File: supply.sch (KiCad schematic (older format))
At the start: 48 parts

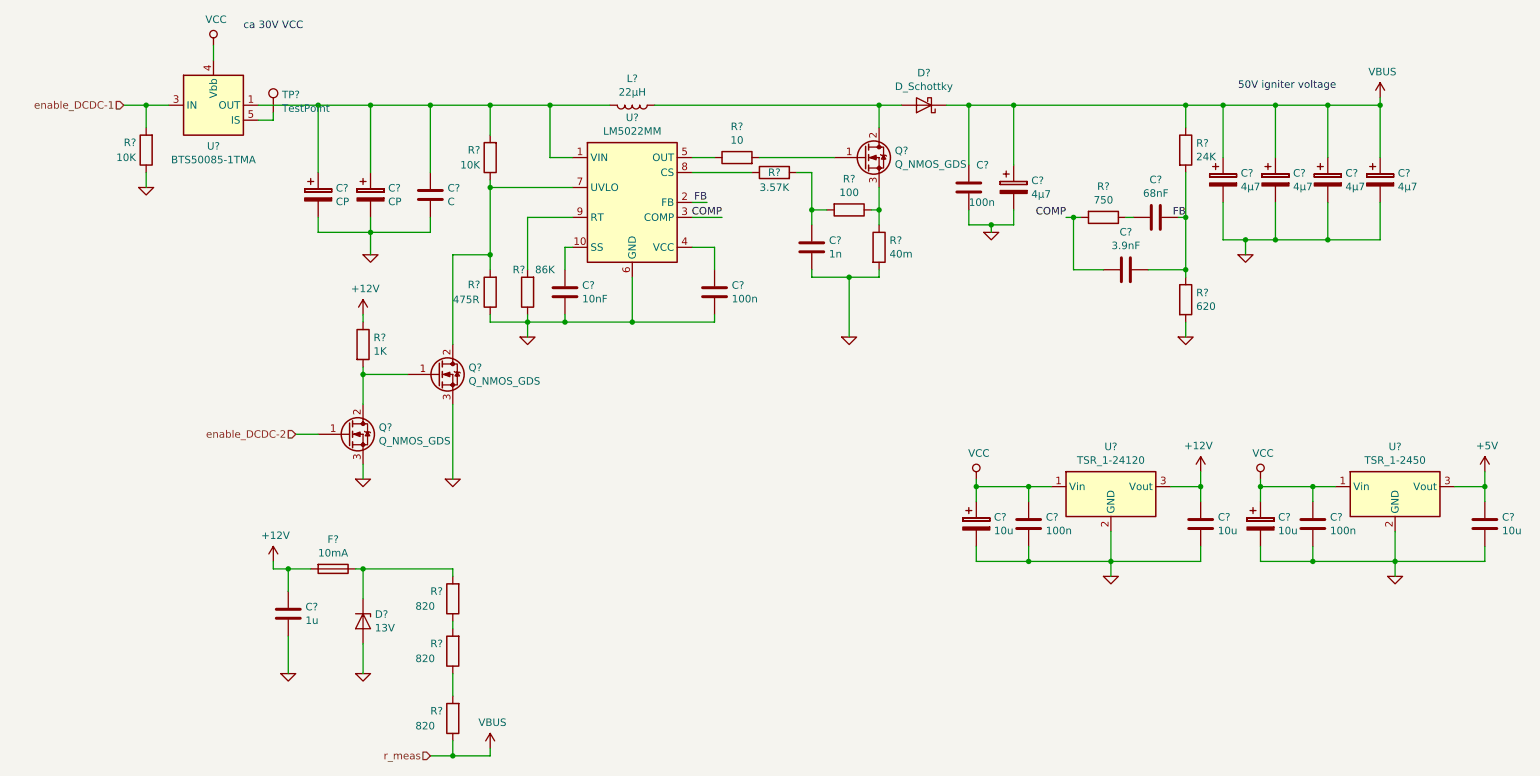
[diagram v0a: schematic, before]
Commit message: updated supply values
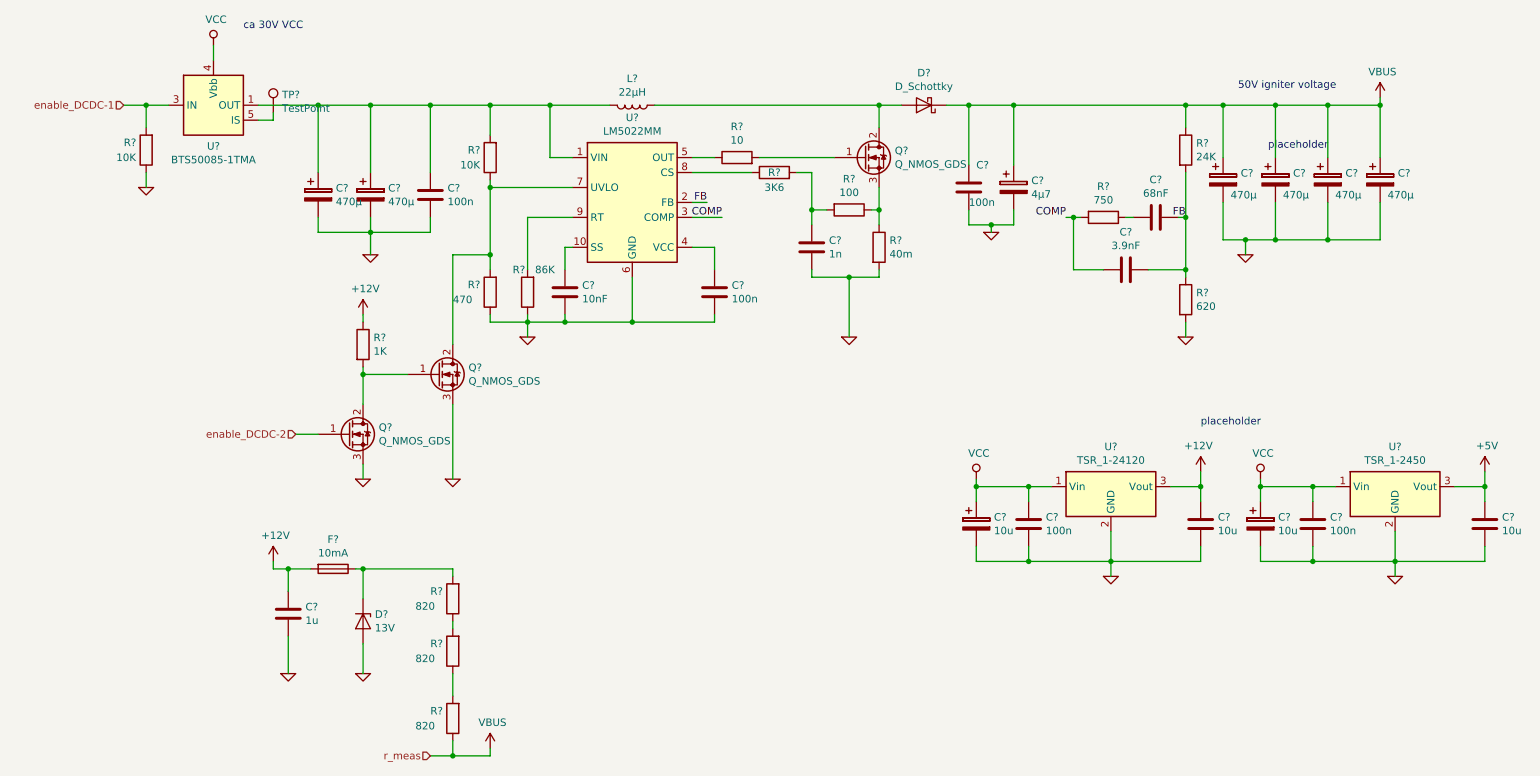
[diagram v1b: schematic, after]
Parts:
- C? (x4): value 4µ7 -> 470µ
- C?: value C -> 100n
- C? (x2): value CP -> 470µ
- R?: value 475R -> 470
- R?: value 3.57K -> 3K6
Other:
- note added: "placeholder\n"
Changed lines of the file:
@@
 P 4150 2450
 F 0 "R?" H 4300 2400 50  0000 R CNN
-F 1 "475R" H 4400 2500 50  0000 R CNN
+F 1 "470" H 4400 2500 50  0000 R CNN
 F 2 "" V 4080 2450 50  0001 C CNN
 F 3 "~" H 4150 2450 50  0001 C CNN
@@
 P 9050 1700
 F 0 "C?" H 9168 1746 50  0000 L CNN
-F 1 "4µ7" H 9168 1655 50  0000 L CNN
+F 1 "470µ" H 9100 1600 50  0000 L CNN
 F 2 "" H 9088 1550 50  0001 C CNN
 F 3 "~" H 9050 1700 50  0001 C CNN
@@
 P 9400 1700
 F 0 "C?" H 9518 1746 50  0000 L CNN
-F 1 "4µ7" H 9518 1655 50  0000 L CNN
+F 1 "470µ" H 9450 1600 50  0000 L CNN
 F 2 "" H 9438 1550 50  0001 C CNN
 F 3 "~" H 9400 1700 50  0001 C CNN
@@
 P 9750 1700
 F 0 "C?" H 9868 1746 50  0000 L CNN
-F 1 "4µ7" H 9868 1655 50  0000 L CNN
+F 1 "470µ" H 9800 1600 50  0000 L CNN
 F 2 "" H 9788 1550 50  0001 C CNN
 F 3 "~" H 9750 1700 50  0001 C CNN
@@
 P 10100 1700
 F 0 "C?" H 10218 1746 50  0000 L CNN
-F 1 "4µ7" H 10218 1655 50  0000 L CNN
+F 1 "470µ" H 10150 1600 50  0000 L CNN
 F 2 "" H 10138 1550 50  0001 C CNN
 F 3 "~" H 10100 1700 50  0001 C CNN
@@
 P 3750 1800
 F 0 "C?" H 3865 1846 50  0000 L CNN
-F 1 "C" H 3865 1755 50  0000 L CNN
+F 1 "100n" H 3865 1755 50  0000 L CNN
 F 2 "" H 3788 1650 50  0001 C CNN
 F 3 "~" H 3750 1800 50  0001 C CNN
@@
 P 3350 1800
 F 0 "C?" H 3468 1846 50  0000 L CNN
-F 1 "CP" H 3468 1755 50  0000 L CNN
+F 1 "470µ" H 3468 1755 50  0000 L CNN
 F 2 "" H 3388 1650 50  0001 C CNN
 F 3 "~" H 3350 1800 50  0001 C CNN
@@
 P 3000 1800
 F 0 "C?" H 3118 1846 50  0000 L CNN
-F 1 "CP" H 3118 1755 50  0000 L CNN
+F 1 "470µ" H 3118 1755 50  0000 L CNN
 F 2 "" H 3038 1650 50  0001 C CNN
 F 3 "~" H 3000 1800 50  0001 C CNN
@@
 P 6050 1650
 F 0 "R?" V 6050 1650 50  0000 C CNN
-F 1 "3.57K" V 5950 1650 50  0000 C CNN
+F 1 "3K6" V 5950 1650 50  0000 C CNN
 F 2 "" V 5980 1650 50  0001 C CNN
 F 3 "~" H 6050 1650 50  0001 C CNN
@@
 	3750 5550 3900 5550
 Connection ~ 3900 5550
+Text Notes 9350 1500 0    50   ~ 0
+placeholder\n
+Text Notes 8900 3350 0    50   ~ 0
+placeholder\n
 $EndSCHEMATC

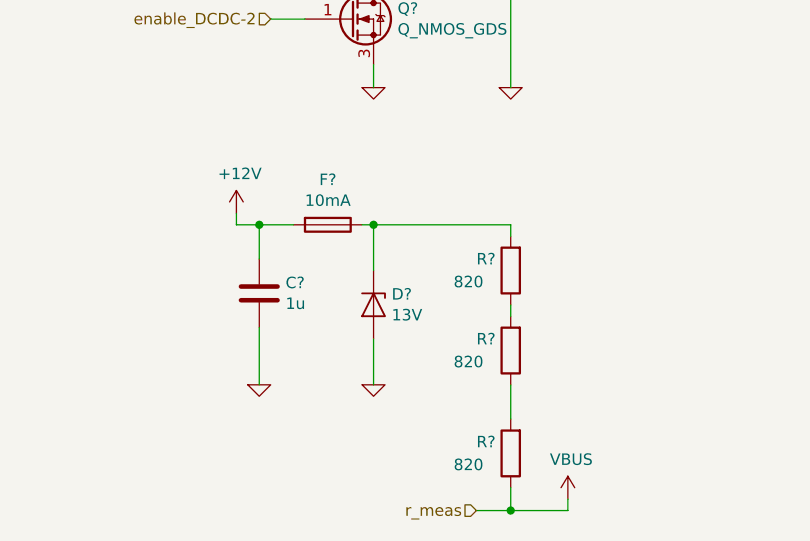
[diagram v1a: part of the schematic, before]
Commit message: added current measurement
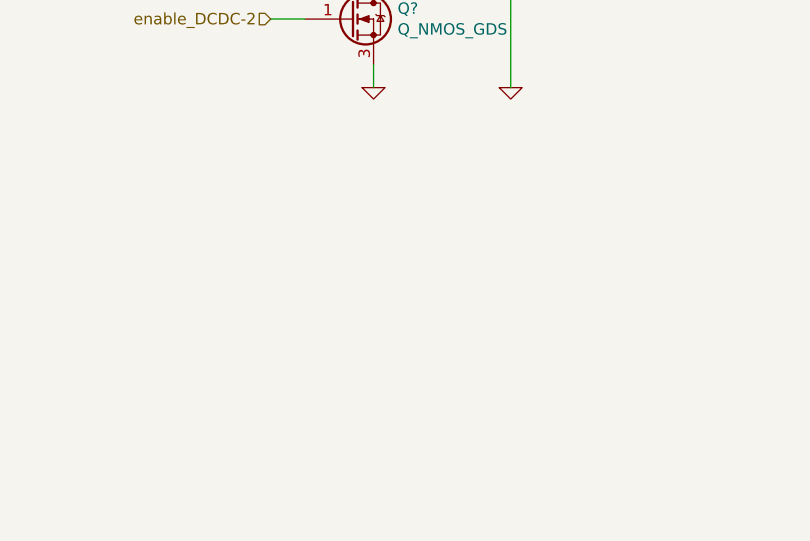
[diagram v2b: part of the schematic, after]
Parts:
- removed C?: 1u, symbol Device:C
- removed D?: 13V, symbol Device:D_Zener
- removed F?: 10mA, symbol Device:Fuse
- removed R? (x3): 820, symbol Device:R
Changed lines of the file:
@@
 $Descr A4 11693 8268
 encoding utf-8
-Sheet 3 4
+Sheet 3 5
 Title ""
 Date ""
@@
 Text HLabel 2850 3400 0    50   Input ~ 0
 enable_DCDC-2
-$Comp
-L Device:R R?
-U 1 1 5D2C7849
-P 3900 4500
-F 0 "R?" H 4050 4450 50  0000 R CNN
-F 1 "820" H 4150 4550 50  0000 R CNN
-F 2 "" V 3830 4500 50  0001 C CNN
-F 3 "~" H 3900 4500 50  0001 C CNN
-	1    3900 4500
-	-1   0    0    1
-$EndComp
-$Comp
-L Device:R R?
-U 1 1 5D2C79C2
-P 3900 4850
-F 0 "R?" H 4050 4800 50  0000 R CNN
-F 1 "820" H 4150 4900 50  0000 R CNN
-F 2 "" V 3830 4850 50  0001 C CNN
-F 3 "~" H 3900 4850 50  0001 C CNN
-	1    3900 4850
-	-1   0    0    1
-$EndComp
-$Comp
-L Device:R R?
-U 1 1 5D2C7AB2
-P 3900 5300
-F 0 "R?" H 4050 5250 50  0000 R CNN
-F 1 "820" H 4150 5350 50  0000 R CNN
-F 2 "" V 3830 5300 50  0001 C CNN
-F 3 "~" H 3900 5300 50  0001 C CNN
-	1    3900 5300
-	-1   0    0    1
-$EndComp
-Wire Wire Line
-	3900 4650 3900 4700
-Wire Wire Line
-	3900 5450 3900 5550
-$Comp
-L power:VBUS #PWR?
-U 1 1 5D2DECB0
-P 4150 5500
-F 0 "#PWR?" H 4150 5350 50  0001 C CNN
-F 1 "VBUS" H 4165 5673 50  0000 C CNN
-F 2 "" H 4150 5500 50  0001 C CNN
-F 3 "" H 4150 5500 50  0001 C CNN
-	1    4150 5500
-	1    0    0    -1
-$EndComp
-$Comp
-L power:+12V #PWR?
-U 1 1 5D2DEF5E
-P 2700 4250
-F 0 "#PWR?" H 2700 4100 50  0001 C CNN
-F 1 "+12V" H 2715 4423 50  0000 C CNN
-F 2 "" H 2700 4250 50  0001 C CNN
-F 3 "" H 2700 4250 50  0001 C CNN
-	1    2700 4250
-	1    0    0    -1
-$EndComp
-$Comp
-L Device:Fuse F?
-U 1 1 5D2DF0C9
-P 3100 4300
-F 0 "F?" V 2903 4300 50  0000 C CNN
-F 1 "10mA" V 2994 4300 50  0000 C CNN
-F 2 "" V 3030 4300 50  0001 C CNN
-F 3 "~" H 3100 4300 50  0001 C CNN
-	1    3100 4300
-	0    1    1    0
-$EndComp
-$Comp
-L Device:D_Zener D?
-U 1 1 5D2DF40E
-P 3300 4650
-F 0 "D?" V 3254 4729 50  0000 L CNN
-F 1 "13V" V 3345 4729 50  0000 L CNN
-F 2 "" H 3300 4650 50  0001 C CNN
-F 3 "~" H 3300 4650 50  0001 C CNN
-	1    3300 4650
-	0    1    1    0
-$EndComp
-Wire Wire Line
-	2700 4300 2700 4250
-Wire Wire Line
-	3250 4300 3300 4300
-Wire Wire Line
-	3900 4300 3900 4350
-Wire Wire Line
-	3300 4500 3300 4300
-$Comp
-L daisy:GND #PWR?
-U 1 1 5D2F9091
-P 3300 5000
-F 0 "#PWR?" H 3300 5000 30  0001 C CNN
-F 1 "GND" H 3300 4930 30  0001 C CNN
-F 2 "" H 3300 5000 60  0000 C CNN
-F 3 "" H 3300 5000 60  0000 C CNN
-	1    3300 5000
-	1    0    0    -1
-$EndComp
-Wire Wire Line
-	3300 4800 3300 5000
-Text HLabel 3750 5550 0    50   Input ~ 0
-r_meas
-Connection ~ 3300 4300
 Text Notes 9150 1100 0    50   ~ 0
 50V igniter voltage\n
@@
 	7400 3700 7400 3750
 Connection ~ 7400 3750
-$Comp
-L Device:C C?
-U 1 1 5D33FD22
-P 2800 4600
-F 0 "C?" H 2915 4646 50  0000 L CNN
-F 1 "1u" H 2915 4555 50  0000 L CNN
-F 2 "" H 2838 4450 50  0001 C CNN
-F 3 "~" H 2800 4600 50  0001 C CNN
-	1    2800 4600
-	1    0    0    -1
-$EndComp
-Wire Wire Line
-	2700 4300 2800 4300
-Wire Wire Line
-	2800 4450 2800 4300
-Connection ~ 2800 4300
-Wire Wire Line
-	2800 4300 2950 4300
-$Comp
-L daisy:GND #PWR?
-U 1 1 5D34E621
-P 2800 5000
-F 0 "#PWR?" H 2800 5000 30  0001 C CNN
-F 1 "GND" H 2800 4930 30  0001 C CNN
-F 2 "" H 2800 5000 60  0000 C CNN
-F 3 "" H 2800 5000 60  0000 C CNN
-	1    2800 5000
-	1    0    0    -1
-$EndComp
-Wire Wire Line
-	2800 4750 2800 5000
-Wire Wire Line
-	3300 4300 3900 4300
-Wire Wire Line
-	4150 5550 4150 5500
-Wire Wire Line
-	3900 5550 4150 5550
-Wire Wire Line
-	3900 5000 3900 5150
-Wire Wire Line
-	3750 5550 3900 5550
-Connection ~ 3900 5550
 Text Notes 9350 1500 0    50   ~ 0
 placeholder\n

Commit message: finished schematic for review
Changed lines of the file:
@@
 Text Notes 9350 1500 0    50   ~ 0
 placeholder\n
-Text Notes 8900 3350 0    50   ~ 0
-placeholder\n
 $EndSCHEMATC

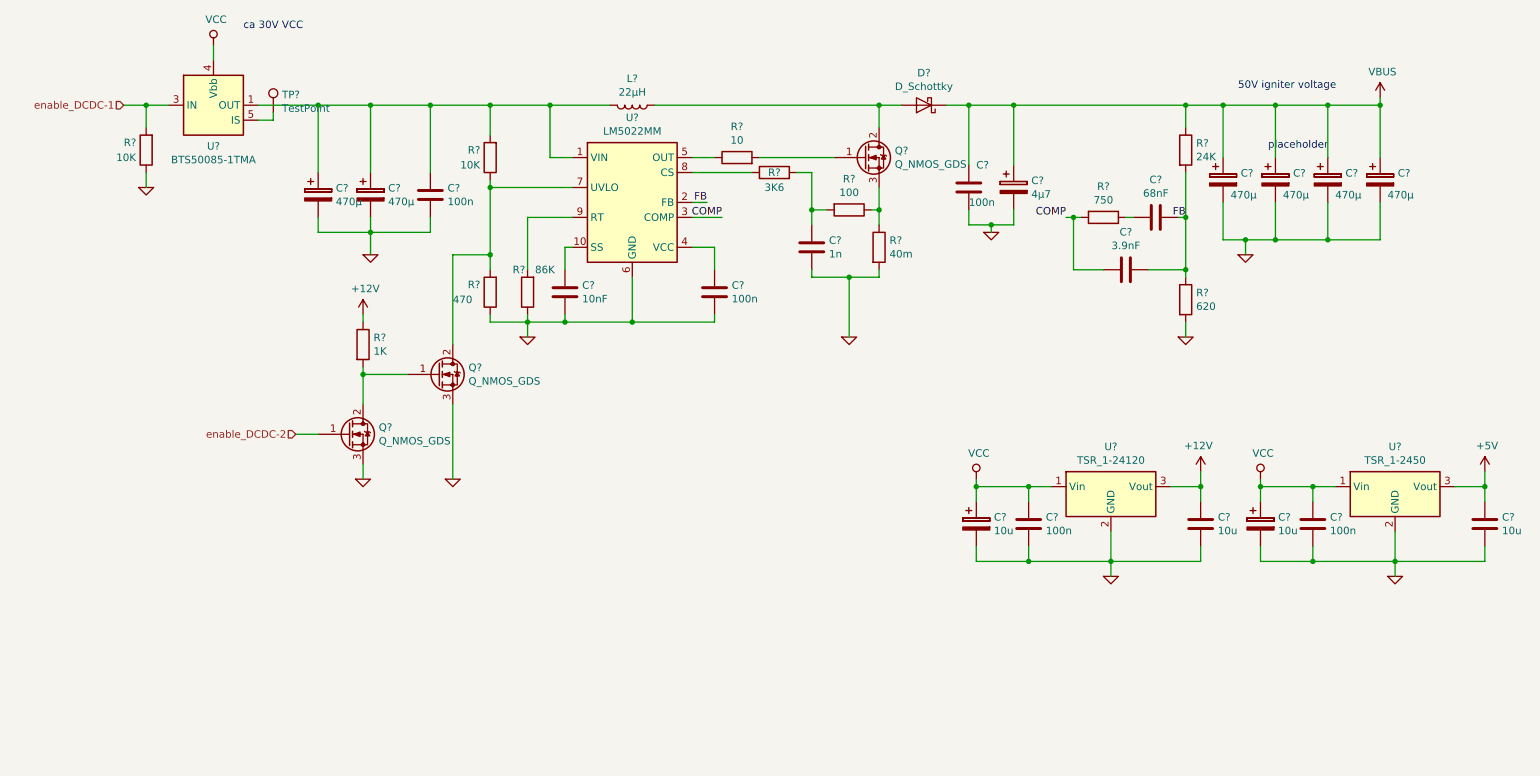
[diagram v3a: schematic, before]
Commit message: added pdf schematic
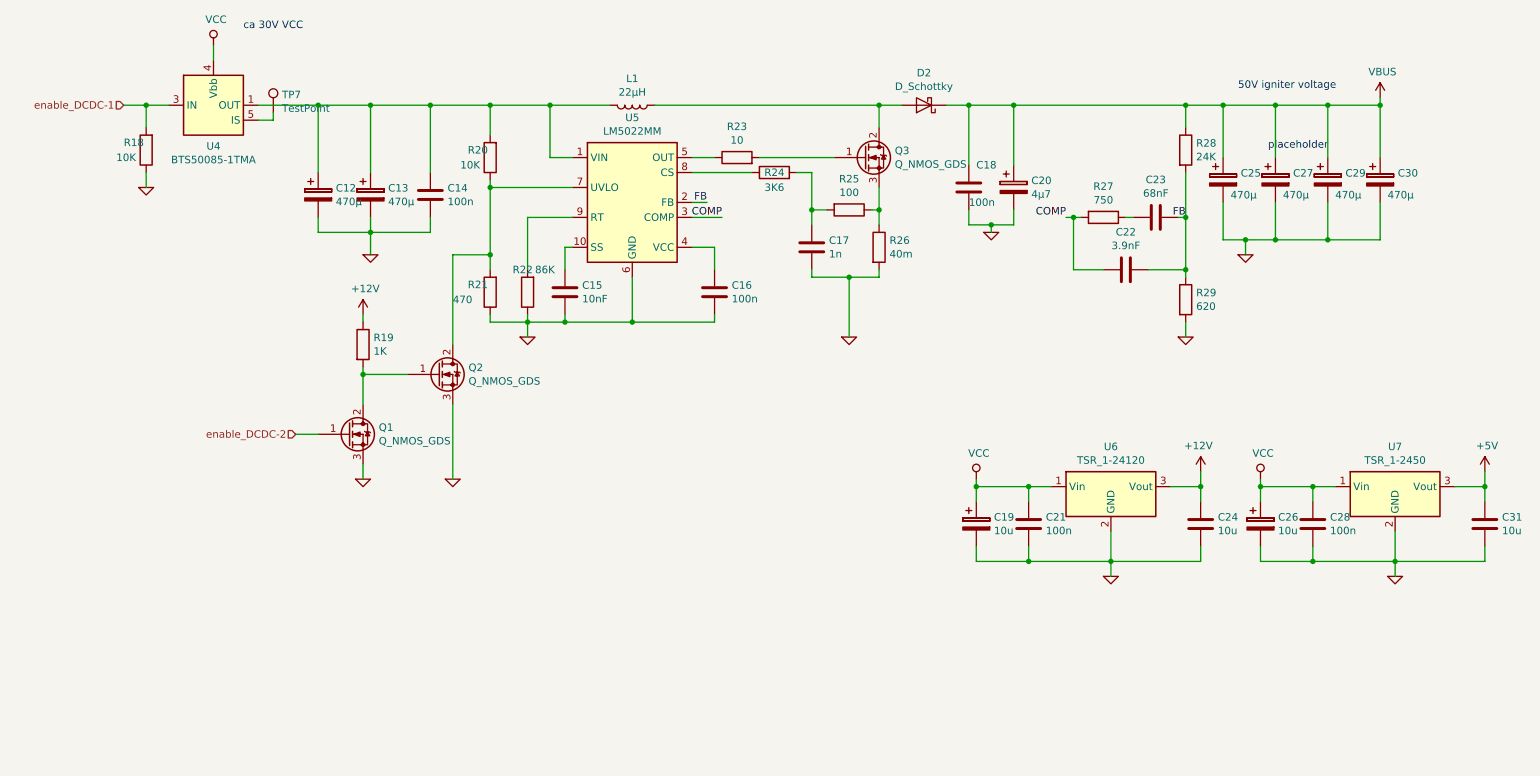
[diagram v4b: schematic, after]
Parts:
- gave numbers to parts that had none: 42
